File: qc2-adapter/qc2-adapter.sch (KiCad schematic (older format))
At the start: 29 parts

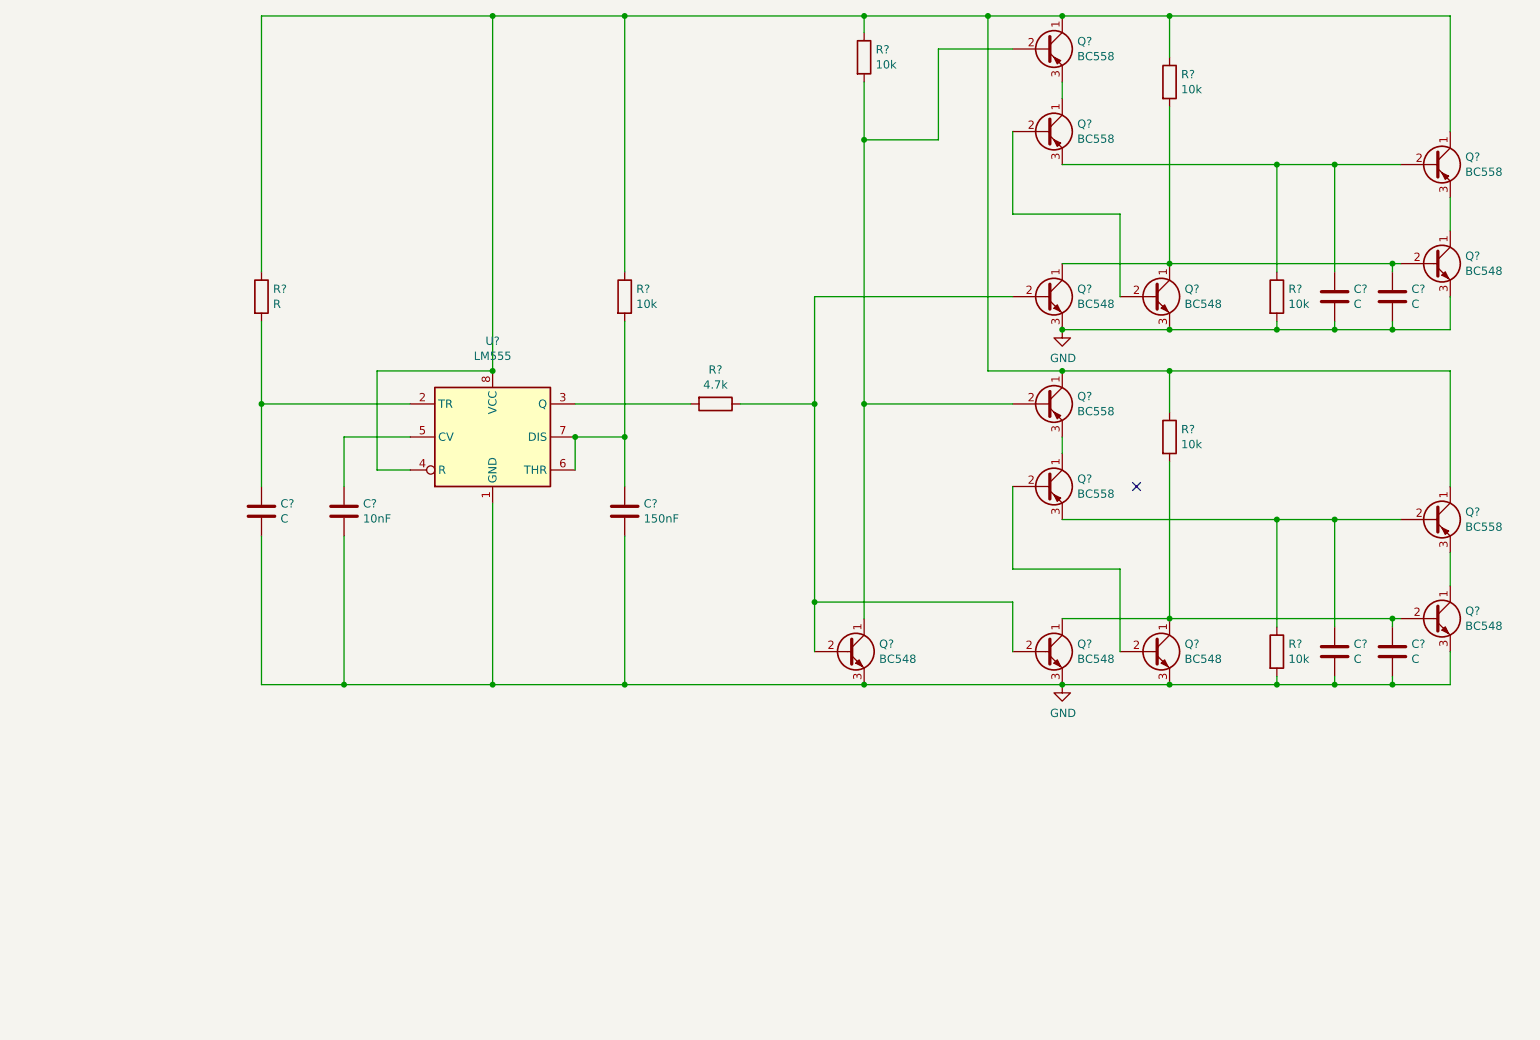
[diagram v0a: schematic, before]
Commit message: qc2-adapter: fix orientation of pnp transistors, remove logically unnecessary parts, add voltage regulator and config jumpers
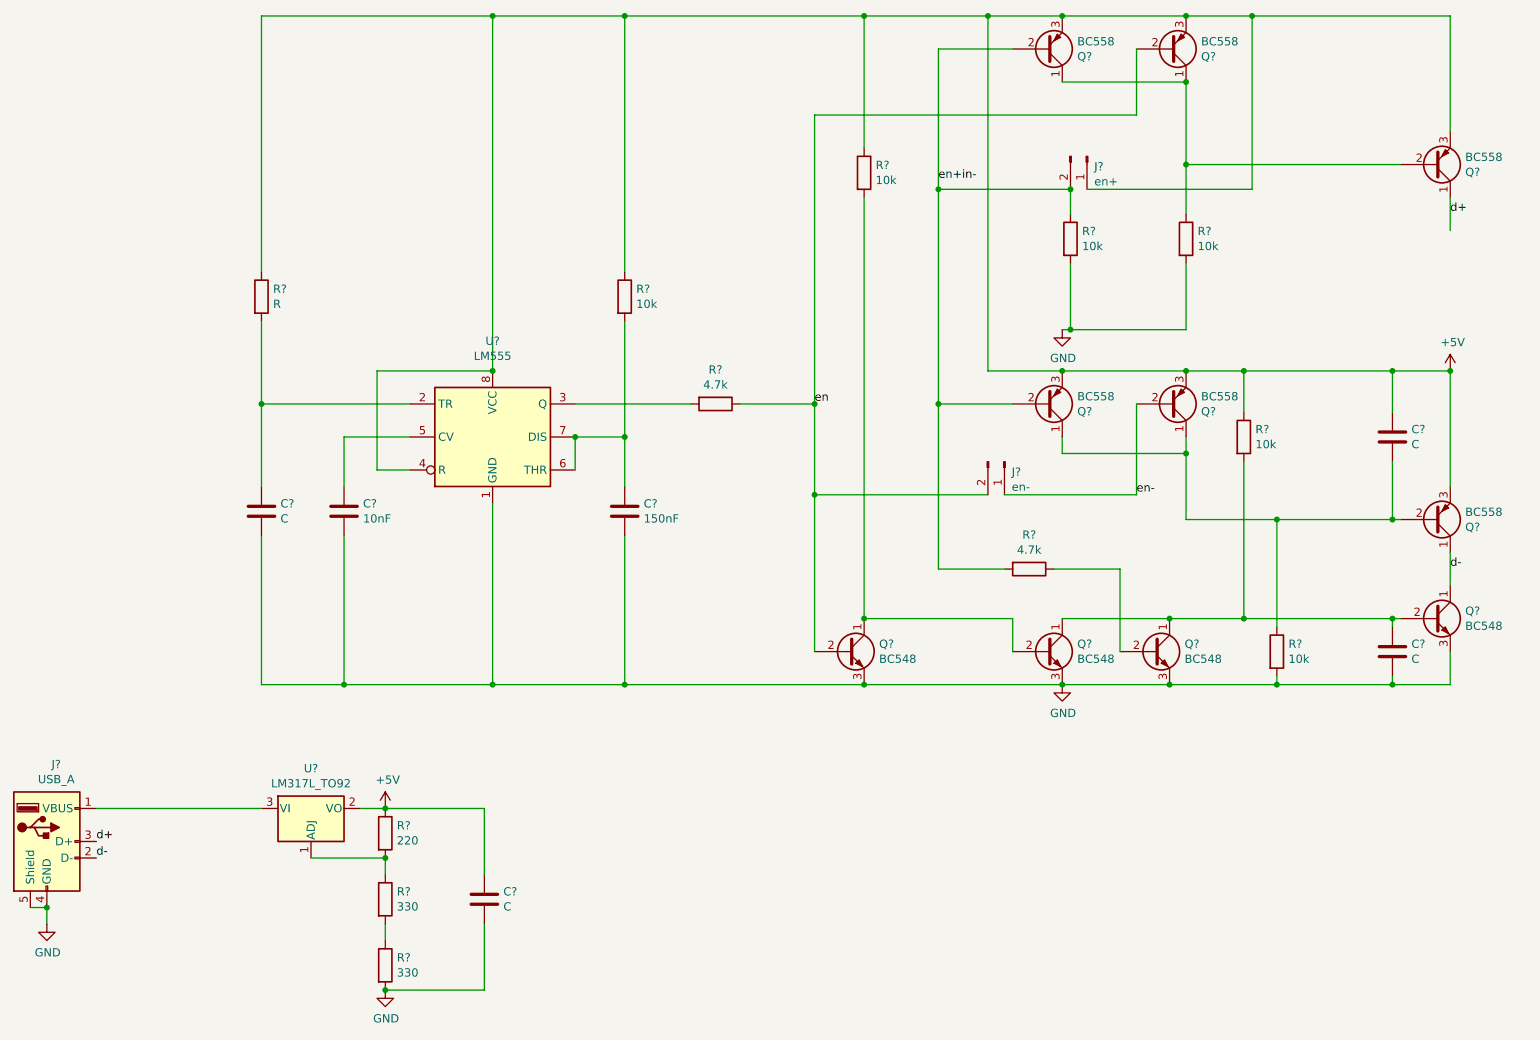
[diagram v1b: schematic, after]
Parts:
- removed C? (x2): C, symbol Device:C
- removed Q? (x3): BC548, Package_TO_SOT_THT:TO-92_Inline, symbol Transistor_BJT:BC548
- removed Q?: BC558, Package_TO_SOT_THT:TO-92_Inline, symbol Transistor_BJT:BC558
- removed R?: 10k, symbol Device:R
- added C?: C, symbol Device:C
- added J?: en-, symbol Connector:Conn_01x02_Male
- added J?: en+, symbol Connector:Conn_01x02_Male
- added J?: USB_A, symbol Connector:USB_A
- added Q?: BC558, Package_TO_SOT_THT:TO-92_Inline, symbol Transistor_BJT:BC558
- added R?: 10k, symbol Device:R
- added R?: 4.7k, symbol Device:R
- added R?: 220, symbol Device:R
- added R? (x2): 330, symbol Device:R
- added U?: LM317L_TO92, Package_TO_SOT_THT:TO-92_Inline, symbol Regulator_Linear:LM317L_TO92
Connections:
- net GND: now also C?.2, J?.4 (GND), J?.5 (Shield), R?.2, R?.2; no longer C?.2
- net +5V: now reaches R?.1, R?.1, R?.1, R?.1, U?.4 (R), U?.8 (VCC)
- net +5V: now also C?.1, Q?.3 (E), Q?.3 (E), Q?.3 (E), Q?.3 (E), Q?.3 (E), C?.1, J?.1 (Pin_1), Q?.3 (E), R?.1, U?.2 (VO); no longer Q?.1 (C), Q?.1 (C), Q?.1 (C), Q?.1 (C)
- net at Q?.2 (B), R?.1: now also Q?.1 (C), Q?.1 (C)
- net at Q?.1 (C), R?.2: now also Q?.2 (B); no longer Q?.2 (B), Q?.2 (B)
- net en: now reaches Q?.2 (B), R?.1
- net en: now also J?.2 (Pin_2), Q?.2 (B); no longer Q?.2 (B)
- net d-: now reaches Q?.1 (C)
- net d-: now also Q?.1 (C), J?.2 (D-); no longer Q?.3 (E)
- net at Q?.1 (C): now also C?.2, Q?.1 (C), Q?.2 (B), R?.1; no longer Q?.3 (E)
- net at Q?.2 (B): now also R?.1; no longer Q?.2 (B)
- new net: J?.1 (VBUS), U?.3 (VI)
- new net: R?.1, R?.2, U?.1 (ADJ)
- new net: R?.1, R?.2
- new net d+: J?.3 (D+), Q?.1 (C)
- new net en+in-: J?.2 (Pin_2), Q?.2 (B), Q?.2 (B), R?.1, R?.2
- new net en-: J?.1 (Pin_1), Q?.2 (B)
- no-connect marks 1 -> 0
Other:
- moved on the sheet: C?, Q?, R?

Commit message: fix USB socket, annotate
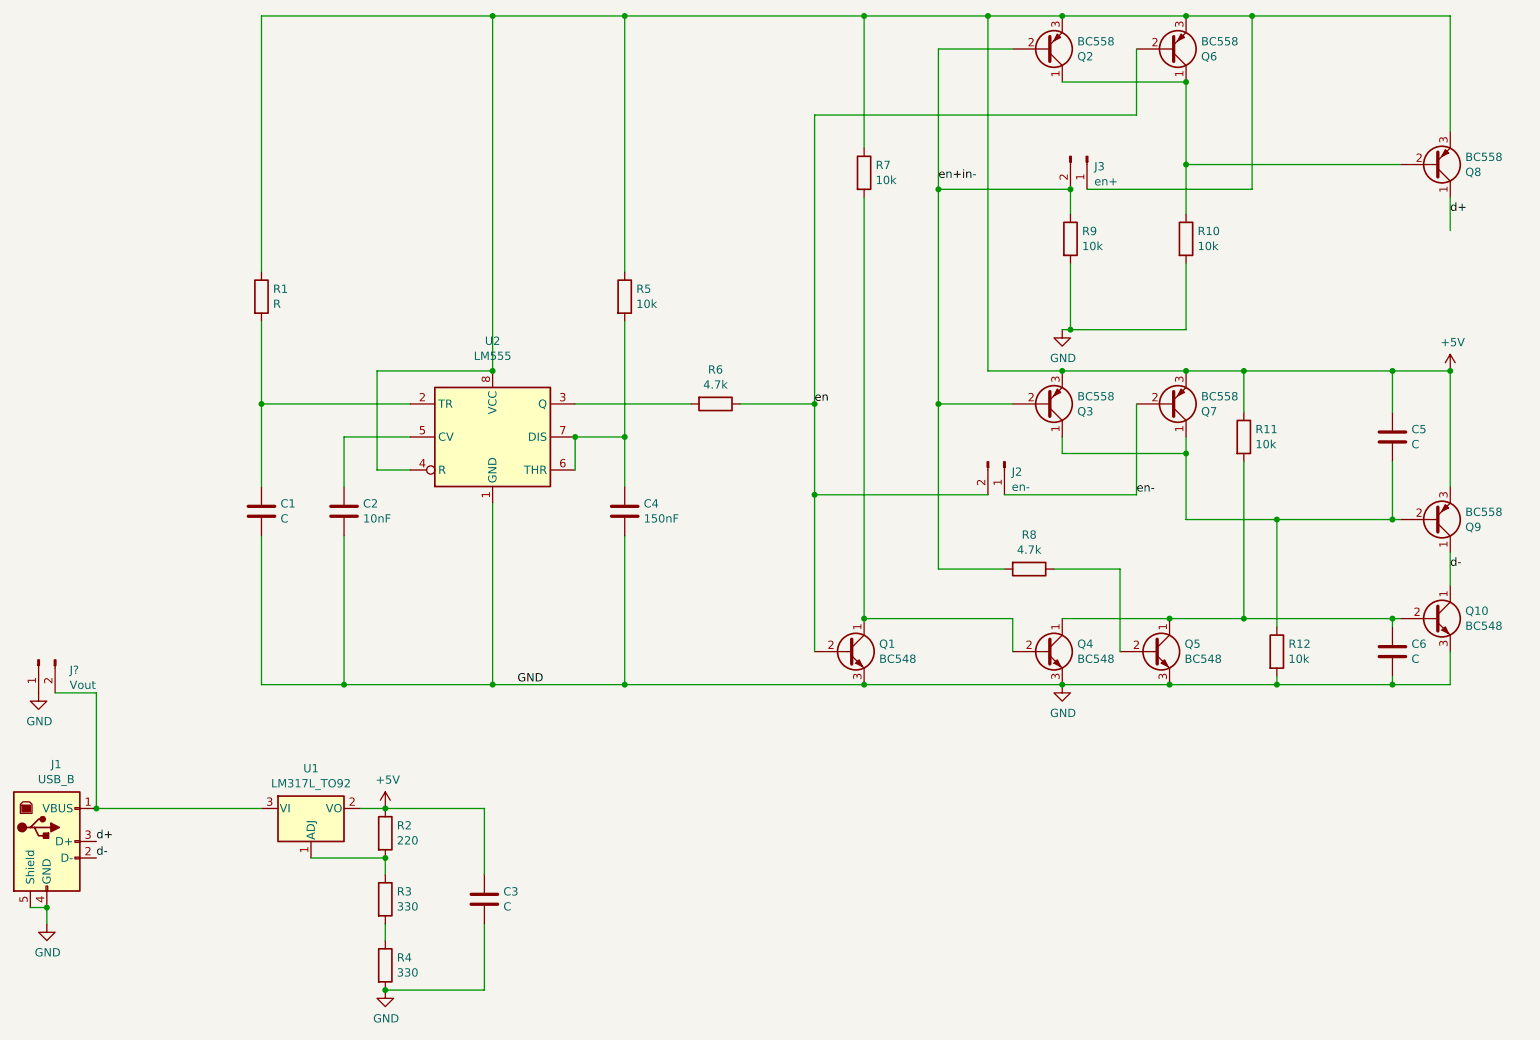
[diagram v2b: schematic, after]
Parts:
- removed J?: USB_A, symbol Connector:USB_A
- added J1: USB_B, symbol Connector:USB_B
- added J?: Vout, symbol Connector:Conn_01x02_Male
- gave numbers to parts that had none: 32
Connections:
- net GND: now also J1.4 (GND), J1.5 (Shield), J?.1 (Pin_1)
- net d+: now also J1.3 (D+)
- net d-: now also J1.2 (D-)
- net at U1.3 (VI): now also J1.1 (VBUS), J?.2 (Pin_2)
